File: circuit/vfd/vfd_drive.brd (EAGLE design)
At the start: 92 x 46 mm, 69 parts, among them J1 ZX62R-AB-5P, J2 2DC-0415D200, J3 FSM-21045-10, J5 PSM-210223-10, Q2 MMSS8050-L, Q3 MMSS8050-L, SW1 SKRPACE010, SW2 SKRPACE010, U1 FT231XS, U2 MAX6921AWI+, U3 NJW4131, U4 DS3231M, U5 ADP3338AKCZ-3.3, U6 PSF-A85, U9 BME280

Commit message: [update]update from thinkpad
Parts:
- removed LED3: VBUS, taki-library:CHIPLED_0603
- removed R10: 1k, taki-library:R0603
- moved C12 162.7 mm to (65.5, -17.5)
- moved C16 162.7 mm to (71.5, -17.5)
- moved C17 162.7 mm to (77.0, -17.5)
- moved LED1 162.7 mm to (83.0, 0.00)
- moved LED2 162.7 mm to (66.5, -7.50)
- moved LED4 162.7 mm to (78.0, -0.50)
- moved Q2 162.7 mm to (67.5, -24.0)
- moved Q3 162.7 mm to (67.5, -31.0)
- moved R12 162.7 mm to (75.0, -6.50)
- moved R13 162.7 mm to (79.5, -6.50)
- moved R14 162.7 mm to (84.0, -6.50)
- moved R15 162.7 mm to (70.5, -6.50)
- moved R16 162.7 mm to (65.5, -12.0)
- moved R17 162.7 mm to (70.0, -12.0)
- moved R18 162.7 mm to (74.5, -12.0)
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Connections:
- removed net N$13: LED3.A, R10.1
- removed net N$17: R10.2
- net GND: no longer LED3.C
- net IO0: now also U6.P$10
- net RESET: now also U6.P$24
- net SDA: now also U6.P$5, U6.P$9

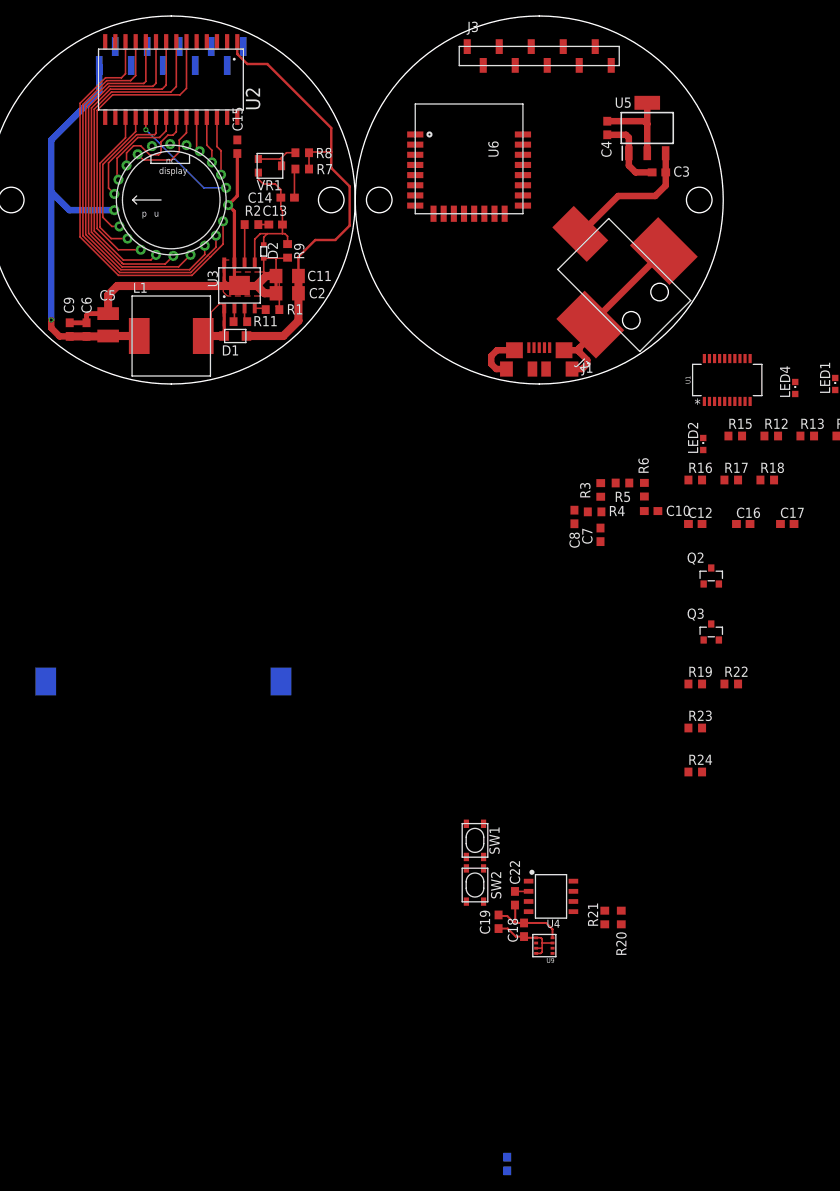
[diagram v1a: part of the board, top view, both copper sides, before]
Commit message: [update]update connector routing
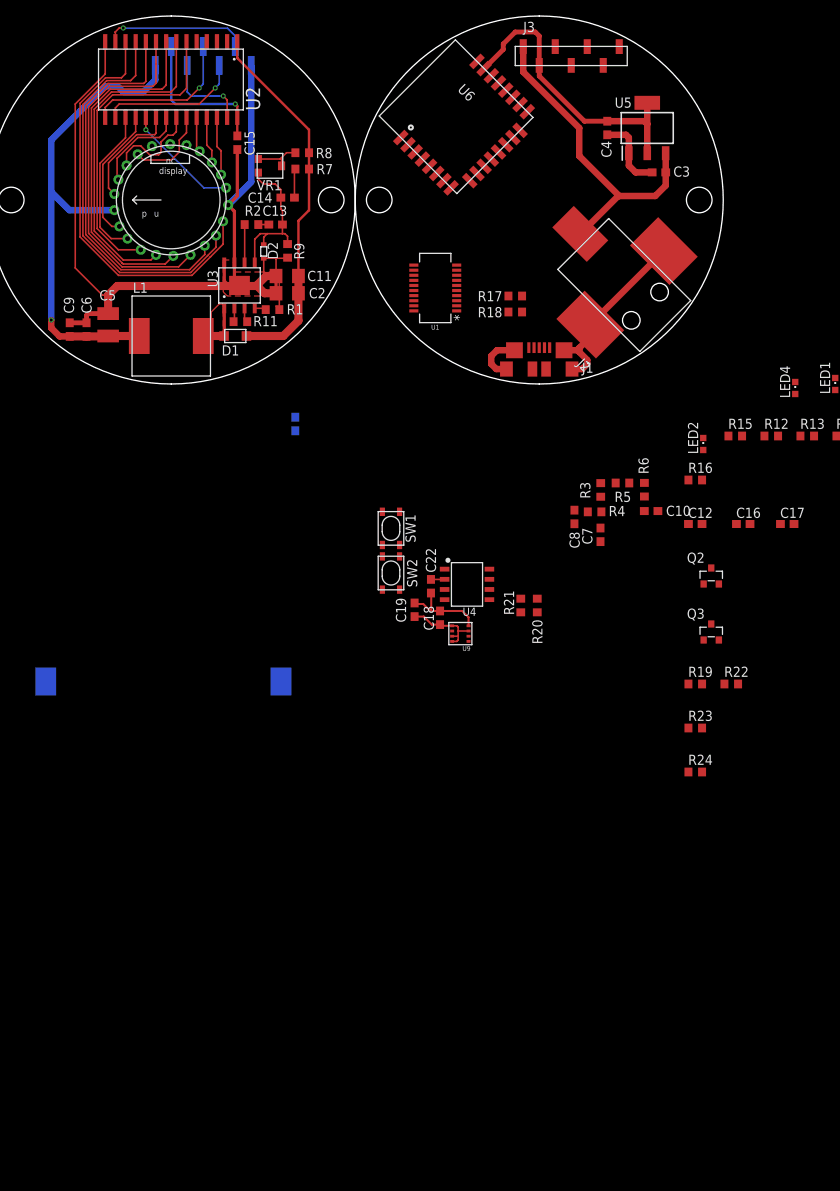
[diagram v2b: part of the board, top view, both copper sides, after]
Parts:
- J3: value FSM-21045-10 -> FSM-21045-7; device taki-library:FSM-21045-10 -> taki-library:FSM-21045-7
- J5: value PSM-210223-10 -> PSM-210223-7; device taki-library:PSM-210223-10 -> taki-library:PSM-210223-7
- moved C1 96.2 mm to (15.5, -5.00), turned to 270 degrees
- moved C22 40.4 mm to (32.5, -25.3)
- moved R20 40.4 mm to (45.8, -27.7)
- moved R21 40.4 mm to (43.7, -27.7)
- moved SW1 40.4 mm to (27.5, -18.0)
- moved SW2 40.4 mm to (27.5, -23.6)
- moved U4 40.4 mm to (37.0, -25.1)
- moved U9 40.4 mm to (36.1, -31.2)
- moved C18 40.4 mm to (33.6, -29.2)
- moved C19 40.4 mm to (30.4, -28.2)
- moved U1 38.3 mm to (33.0, 12.0), turned to 90 degrees
- moved R18 37.9 mm to (43.0, 9.00), turned to 180 degrees
- moved R17 35.5 mm to (43.0, 11.0), turned to 180 degrees
- moved J3 7.00 mm to (44.0, 41.0)
- moved J5 7.00 mm to (-2.00, 41.0)
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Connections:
- net +3V3: now also J3.2
- net +5V: now also J3.1
- net GND: now also J3.7, J5.7
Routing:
- net GND: track 122.3 -> 176.8 mm
- net +5V: track 74.6 -> 105.0 mm
- net +3V3: track 23.9 -> 49.1 mm
- net N$4: track 0.00 -> 19.3 mm, vias 0 -> 1
- net N$2: track 0.00 -> 19.0 mm, vias 0 -> 1
- net N$18: track 0.00 -> 18.2 mm, vias 0 -> 1
- net N$5: track 0.00 -> 17.7 mm, vias 0 -> 1
- net +24V: track 58.4 -> 46.5 mm
- net N$3: track 0.00 -> 10.9 mm, vias 0 -> 1

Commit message: [complete]complete vfd driver board
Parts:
- removed LED4: VBUS, taki-library:CHIPLED_0603
- removed Q3: MMSS8050-L, taki-library:SOT23
- removed R14: 1k, taki-library:R0603
- removed R15: 4.7k, taki-library:R0603
- removed R16, R19, R22: 10k, taki-library:R0603
- removed R4, R6: 470, taki-library:R0603
- added J4: PSM-210223-7, taki-library:PSM-210223-7
- added J6: FSM-21045-7, taki-library:FSM-21045-7
- added Q1: BSS138, taki-library:SOT23-N-MOSFET
- added R10, R25: 4.7k, taki-library:R0603
- C10: value 1000pF -> 0.1uF
- Q2: value MMSS8050-L -> BSS138; device taki-library:SOT23 -> taki-library:SOT23-N-MOSFET
- moved R24 85.9 mm to (25.7, 27.6)
- moved R23 71.1 mm to (35.8, 21.6), turned to 135 degrees
- moved C10 60.9 mm to (40.1, 41.6), turned to 135 degrees
- moved R20 54.7 mm to (31.3, 25.0), turned to 315 degrees
- moved Q2 53.3 mm to (45.5, 24.5)
- moved R21 51.1 mm to (41.3, 23.3), turned to 0 degrees
- moved R13 45.4 mm to (36.7, 8.80), turned to 90 degrees
- moved LED1 44.3 mm to (38.8, 3.49), turned to 180 degrees
- moved R3 44.3 mm to (48.7, 30.8)
- moved R5 44.2 mm to (46.6, 30.7), turned to 90 degrees
- moved U4 42.8 mm to (29.5, 17.1), turned to 90 degrees
- moved C22 42.6 mm to (34.0, 17.3), turned to 90 degrees
- moved C17 42.2 mm to (43.4, 8.02), turned to 180 degrees
- moved C1 41.9 mm to (-13.4, 25.3), flipped to the top
- moved C19 40.0 mm to (30.7, 11.7), turned to 180 degrees
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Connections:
- removed net N$11: LED4.A, R14.1
- removed net N$12: C10.2, R6.1, SW2.S1, SW2.S2
- removed net N$14: R15.1, R16.2, U1.18
- removed net N$15: Q2.B, R19.1
- removed net N$16: Q3.B, R22.1
- removed net N$2: C15.1, J5.2, U2.28
- removed net N$6: C8.2, R4.1, SW1.S1, SW1.S2
- new net 32KHZ: R10.1, U4.1, U6.P$6
- new net SQW: R25.1, U4.3, U6.P$7
- new net SW1: J4.2
- new net SW2: J4.3
- new net SW3: J4.4
- new net SW4: J4.5
- new net VFBLANK: J3.6, U6.P$11
- new net VFCLK: J3.4, U6.P$14
- new net VFDIN: J3.3, U6.P$15
- new net VFLOAD: J3.5, U6.P$13
- net +3V3: now also C10.1, C15.1, J4.1, J5.2, J6.1, R10.2, R25.2, U2.28
- net DTR: now also Q1.G, Q2.S; no longer Q3.E, R19.2
- net GND: now also C10.2, J4.7, J6.7; no longer C10.1, C7.2, C8.1, LED4.C, R16.1, SW1.P1, SW1.P2, SW2.P1, SW2.P2
- net IO0: now also Q2.D; no longer Q3.C, R6.2
- net RESET: now also Q1.D; no longer C7.1, Q2.C, R4.2
- net RTS: now also Q1.S, Q2.G; no longer Q2.E, R22.2
- net SCL: now also U6.P$5
- net SDA: no longer U6.P$5
- net VBATT: now also J4.6
- net VBUS: no longer R14.2, R15.2
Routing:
- net GND: track 176.8 -> 348.4 mm, vias 0 -> 11
- net +3V3: track 49.1 -> 182.4 mm, vias 0 -> 13
- net VBATT: track 0.00 -> 51.5 mm, vias 0 -> 1
- net VFBLANK: track 0.00 -> 36.7 mm, vias 0 -> 2
- net SDA: track 0.00 -> 32.8 mm, vias 0 -> 2
- net SCL: track 0.06 -> 31.2 mm
- net RESET: track 0.00 -> 26.3 mm, vias 0 -> 2
- net TXD: track 0.00 -> 26.0 mm, vias 0 -> 2
- net +5V: track 105.0 -> 129.6 mm
- net 32KHZ: track 0.00 -> 22.5 mm, vias 0 -> 2
- net VFLOAD: track 0.00 -> 22.3 mm, vias 0 -> 2
- net RXD: track 0.00 -> 21.2 mm, vias 0 -> 2
- net N$8: track 0.00 -> 20.4 mm, vias 0 -> 2
- net N$7: track 0.00 -> 20.1 mm, vias 0 -> 2
- net N$2: track 19.0 -> 0.00 mm, vias 1 -> 0
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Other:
- board size 92 x 46 mm -> 92 x 92 mm

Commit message: [update] draw outline
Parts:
- added C20, C21, C23, C24: 1000pF, taki-library:C0603
- added R14, R15, R4, R6: 10k, taki-library:R0603
- added SW3, SW4, SW5, SW6: JTP1230D, taki-library:JTP1230D
- moved SW2 109.9 mm to (85.0, 86.3)
- moved SW1 107.2 mm to (85.0, 79.4)
- moved C7 98.6 mm to (88.2, 82.6), turned to 0 degrees
- moved C8 96.3 mm to (89.1, 77.6), turned to 270 degrees
- moved J6 68.6 mm to (21.5, 40.5)
- moved C4 64.4 mm to (88.0, 87.0)
- moved U5 64.4 mm to (93.0, 87.0)
- moved C3 64.4 mm to (94.5, 81.5)
- moved C22 62.3 mm to (65.0, 71.3)
- moved C18 62.3 mm to (61.7, 62.7)
- moved C10 62.3 mm to (71.1, 95.6)
- moved C12 62.3 mm to (73.1, 68.7)
- moved C16 62.3 mm to (77.4, 62.0)
- moved C17 62.3 mm to (74.4, 62.0)
- moved J1 62.3 mm to (77.0, 55.9)
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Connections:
- new net N$2: BATT1.P, J6.6
- new net SW1-SW: C20.2, J6.2, R4.1, SW3.3, SW3.4
- new net SW2-SW: C21.2, J6.3, R6.1, SW4.3, SW4.4
- new net SW3-SW: C23.2, J6.4, R14.1, SW5.3, SW5.4
- new net SW4-SW: C24.2, J6.5, R15.1, SW6.3, SW6.4
- net +3V3: now also R14.2, R15.2, R4.2, R6.2
- net GND: now also C20.1, C21.1, C23.1, C24.1, C7.2, C8.1, SW1.P1, SW1.P2, SW2.P1, SW2.P2, SW3.1, SW3.2, SW4.1, SW4.2, SW5.1, SW5.2, SW6.1, SW6.2
- net IO0: now also C7.1, SW2.S1, SW2.S2
- net RESET: now also C8.2, SW1.S1, SW1.S2
- net SW1: now also U6.P$19
- net SW2: now also U6.P$18
- net SW3: now also U6.P$17
- net SW4: now also U6.P$16
- net VBATT: no longer BATT1.P
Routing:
- net GND: track 348.4 -> 377.4 mm
- net IO0: track 12.5 -> 30.7 mm, vias 0 -> 4
- net SW4: track 0.00 -> 15.0 mm, vias 0 -> 3
- net RESET: track 26.3 -> 40.9 mm, vias 2 -> 4
- net SW3: track 0.00 -> 11.9 mm, vias 0 -> 1
- net SW1: track 0.00 -> 10.5 mm, vias 0 -> 1
- net SW2: track 0.00 -> 8.37 mm, vias 0 -> 1
- net +3V3: track 182.4 -> 190.2 mm
- net +5V: track 129.6 -> 134.0 mm
- net VFDIN: track 16.5 -> 17.7 mm
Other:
- board size 92 x 92 mm -> 100 x 100 mm
- board text added: "IO0"
- board text added: "RST"

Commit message: [update] update vfd
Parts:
- moved R4 34.5 mm to (30.6, 10.3), turned to 180 degrees
- moved C23 33.2 mm to (41.7, 31.1), turned to 90 degrees
- moved C20 32.6 mm to (41.6, 15.1), turned to 90 degrees
- moved C24 30.3 mm to (4.30, 31.0), turned to 90 degrees
- moved R6 20.7 mm to (16.3, 10.3)
- moved R14 18.4 mm to (32.3, 35.7), turned to 180 degrees
- moved R15 16.1 mm to (13.6, 35.7)
- moved C21 12.7 mm to (4.31, 15.0), turned to 90 degrees
- moved SW5 11.4 mm to (36.5, 31.0), flipped to the bottom
- moved SW3 8.63 mm to (36.5, 15.0), flipped to the bottom
- moved SW4 3.35 mm to (9.50, 15.0), flipped to the bottom
- moved SW6 2.06 mm to (9.50, 31.0), flipped to the bottom
- moved J6 0.71 mm to (21.0, 41.0)
- moved BATT1 0.52 mm to (23.0, 23.0)
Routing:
- net GND: track 377.4 -> 513.0 mm, vias 11 -> 122
- net +3V3: track 190.2 -> 252.8 mm, vias 13 -> 15
- net SW2-SW: track 0.00 -> 54.4 mm, vias 0 -> 3
- net SW1-SW: track 0.00 -> 49.0 mm, vias 0 -> 3
- net SW4-SW: track 0.00 -> 36.5 mm
- net N$2: track 0.00 -> 24.9 mm, vias 0 -> 2
- net SW3-SW: track 0.00 -> 21.6 mm
- added copper zone on layer 16, net GND

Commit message: [add]add silk
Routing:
- net GND: vias 122 -> 131
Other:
- board text added: "Designed by Kinoshita(@_nosita)"
- board text added: "Nostalgy"
- board text added: "nittc meister2018"
- board text added: "vfd tube drive board rev.2"
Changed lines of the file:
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@@
 <dimension x1="23" y1="46" x2="23" y2="54" x3="14" y3="50" textsize="1.778" layer="47"/>
 <dimension x1="23" y1="46" x2="23" y2="0" x3="-8" y3="23" textsize="1.778" layer="47"/>
+<hole x="4" y="85" drill="3.2"/>
+<text x="17.5" y="6.5" size="2.1844" layer="21">Nostalgy</text>
+<text x="13.5" y="4.5" size="1.016" layer="21">Designed by Kinoshita(@_nosita)</text>
+<text x="15.5" y="3" size="1.016" layer="21">vfd tube drive board rev.2</text>
+<text x="18" y="1.5" size="1.016" layer="21">nittc meister2018</text>
 </plain>
 <attributes>
@@
 <via x="4.5" y="73.5" extent="1-16" drill="0.3048"/>
 <via x="4.5" y="81.5" extent="1-16" drill="0.3048"/>
-<via x="4.5" y="85" extent="1-16" drill="0.3048"/>
 <via x="8.5" y="90" extent="1-16" drill="0.3048"/>
 <via x="12" y="93.5" extent="1-16" drill="0.3048"/>
@@
 <vertex x="28.5" y="65.5"/>
 </polygon>
-<wire x1="57.73" y1="72.955" x2="37.54" y2="69.79" width="0" layer="19" extent="1-1"/>
 <via x="13" y="66.5" extent="1-16" drill="0.3048"/>
 <via x="26.5" y="66.5" extent="1-16" drill="0.3048"/>
@@
 <via x="11" y="68" extent="1-16" drill="0.3048"/>
 <via x="4.5" y="71.5" extent="1-16" drill="0.3048"/>
+<via x="69" y="84" extent="1-16" drill="0.3048"/>
+<via x="85.5" y="67.5" extent="1-16" drill="0.3048"/>
+<via x="86.5" y="68" extent="1-16" drill="0.3048"/>
+<via x="87" y="69" extent="1-16" drill="0.3048"/>
+<via x="88" y="68" extent="1-16" drill="0.3048"/>
+<via x="87.5" y="67" extent="1-16" drill="0.3048"/>
+<via x="86.5" y="66.5" extent="1-16" drill="0.3048"/>
+<via x="87.5" y="65.5" extent="1-16" drill="0.3048"/>
+<via x="88.5" y="66" extent="1-16" drill="0.3048"/>
+<via x="89" y="67" extent="1-16" drill="0.3048"/>
+<wire x1="33" y1="42.175" x2="36.5" y2="62" width="0" layer="19" extent="1-1"/>
 </signal>
 <signal name="VBUS">

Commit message: [add]add all
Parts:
- added U$1: (no value), 180118 Library by matsu:HAZAMARU
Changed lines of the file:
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@@
 <dimension x1="23" y1="46" x2="23" y2="54" x3="14" y3="50" textsize="1.778" layer="47"/>
 <dimension x1="23" y1="46" x2="23" y2="0" x3="-8" y3="23" textsize="1.778" layer="47"/>
-<hole x="4" y="85" drill="3.2"/>
+<hole x="5" y="85" drill="3.2"/>
 <text x="17.5" y="6.5" size="2.1844" layer="21">Nostalgy</text>
 <text x="13.5" y="4.5" size="1.016" layer="21">Designed by Kinoshita(@_nosita)</text>
 <text x="15.5" y="3" size="1.016" layer="21">vfd tube drive board rev.2</text>
 <text x="18" y="1.5" size="1.016" layer="21">nittc meister2018</text>
+<hole x="77" y="43" drill="3.2"/>
+<circle x="77" y="43" radius="3" width="0.0762" layer="47"/>
 </plain>
 <attributes>
@@
 <attribute name="NAME" x="3.458" y="29.351" size="1.27" layer="25" rot="R90"/>
 </element>
+<element name="U$1" library="180118 Library by matsu" package="HAZAMARU" value="" x="66.5" y="13" smashed="yes"/>
 </elements>
 <signals>

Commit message: [add]add all
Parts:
- removed BATT1: SMTU2032, taki-library:SMTU2032
- removed C18, C19, C22: 0.1uF, taki-library:C0603
- removed C20, C21, C23, C24: 1000pF, taki-library:C0603
- removed D1: SS2040FL, taki-library:SOD-123FL
- removed D2: BZX584C3V9, taki-library:SOD-523
- removed J2: 2DC-0415D200, taki-library:2DC-0415D200
- removed J4: PSM-210223-7, taki-library:PSM-210223-7
- removed J6: FSM-21045-7, taki-library:FSM-21045-7
- removed LED1: RX, taki-library:CHIPLED_0603
- removed LED2: TX, taki-library:CHIPLED_0603
- removed R12, R13: 1k, taki-library:R0603
- removed R14, R15, R23, R24, R4, R6: 10k, taki-library:R0603
- removed R17, R18: 27, taki-library:R0603
- removed R20, R21, R25: 4.7k, taki-library:R0603
- removed SW1, SW2: SKRPACE010, taki-library:SKRPACE010
- removed SW3, SW4, SW5, SW6: JTP1230D, taki-library:JTP1230D
- removed U$1: (no value), 180118 Library by matsu:HAZAMARU
- removed U4: DS3231M, taki-library:SO08
- removed U9: BME280, taki-library:LGA-8-2.5X2.5
- added J7: DC_JACK_2DC0005D100, taki-library:DC_JACK_2DC0005D100
- added U8: ESP-WROOM-32, taki-library:ESP-WROOM-32
- C10: value 0.1uF -> 5uF
- C12: value 0.1uF -> 1500pF
- C13: value 10uF -> 680pF
- C14: value 270pF -> 100uF; device taki-library:C0603 -> taki-library:C1206
- C16: value 47pF -> 1uF
- C17: value 47pF -> 0.1uF
- C7: value 1000pF -> 1uF
- C8: value 1000pF -> 4.7uF
- L1: value NR10050T470M -> NR10050T221M
- R1: value 27k -> 220
- R10: value 4.7k -> 47k
- R11: value 27k -> 10k
- R2: value 8.2k -> 0.02; device taki-library:R0603 -> taki-library:R1206
- R7: value 27k -> 24k
- U1: value FT231XS -> CP2104; device taki-library:SSOP20_L -> taki-library:QFN24-SILABS
- U3: value NJW4131 -> NJM2360AM; device taki-library:HSOP8 -> taki-library:DMP8
- U6: value PSF-A85 -> RX8035LC; device ITEAD:PSF-A85 -> taki-library:VSOJ12
- moved C17 106.1 mm to (-9.50, -3.00), turned to 0 degrees
- moved C13 64.4 mm to (-25.7, 55.6), turned to 180 degrees
- moved L1 56.1 mm to (-32.5, 68.0)
- moved C2 55.6 mm to (-18.0, 69.3)
- moved C11 55.5 mm to (-18.0, 67.0)
- moved U3 53.7 mm to (-22.0, 62.0)
- moved R1 52.7 mm to (-17.0, 63.3), turned to 270 degrees
- moved R7 49.4 mm to (84.0, 59.7)
- moved R2 45.4 mm to (-7.00, 52.5), turned to 0 degrees
- moved R11 40.2 mm to (71.7, 65.4), turned to 45 degrees
- moved C10 33.0 mm to (73.0, 62.6), turned to 0 degrees
- moved U6 27.5 mm to (84.5, 88.0), turned to 180 degrees
- moved C5 26.8 mm to (-11.6, 59.4), turned to 0 degrees
- moved C7 26.8 mm to (73.0, 60.6)
- moved C8 26.7 mm to (65.8, 64.7), turned to 45 degrees
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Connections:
- removed net 32KHZ: R10.1, U4.1, U6.P$6
- removed net D2_N: R17.2, U1.12
- removed net D2_P: R18.2, U1.11
- removed net D_N1: C16.1, J1.D-, R17.1
- removed net D_P1: C17.1, J1.D+, R18.1
- removed net N$10: LED2.A, R13.1
- removed net N$19: R23.2, U6.P$8
- removed net N$21: R24.1, U6.P$3
- removed net N$40: R1.2, U3.4
- removed net N$41: D1.A, L1.P$2, U3.1
- removed net N$43: R2.2, U3.6
- removed net N$46: C13.1, R2.1
- removed net N$47: C13.2, C14.1, D2.K, R9.2, U3.5, VR1.3
- removed net N$48: C14.2, R7.2
- removed net N$49: R8.2, VR1.1, VR1.2
- removed net RESET: C8.2, Q1.D, R3.1, SW1.S1, SW1.S2, U6.P$24
- removed net RXD: U1.4, U6.P$22
- removed net SQW: R25.1, U4.3, U6.P$7
- removed net SW1: J4.2, U6.P$19
- removed net SW1-SW: C20.2, J6.2, R4.1, SW3.3, SW3.4
- removed net SW2: J4.3, U6.P$18
- removed net SW2-SW: C21.2, J6.3, R6.1, SW4.3, SW4.4
- removed net SW3: J4.4, U6.P$17
- removed net SW3-SW: C23.2, J6.4, R14.1, SW5.3, SW5.4
- removed net SW4: J4.5, U6.P$16
- removed net SW4-SW: C24.2, J6.5, R15.1, SW6.3, SW6.4
- removed net TXD: U1.20, U6.P$21
- removed net VBATT: J4.6, U4.6
- new net D_N: J1.D-, U1.4
- new net D_P: J1.D+, U1.3
- new net EN: C12.1, Q1.D, R3.1, U8.3
- new net ESP32_RX: U1.21, U8.35
- new net ESP32_TX: U1.20, U8.34
- new net N$11: C13.1, U3.3
- new net N$12: R8.2, U3.5, VR1.1, VR1.2
- new net N$13: R1.1, U3.8
- new net N$14: L1.P$1, R1.2, R2.2, U3.7
- new net N$6: L1.P$2, U3.1
- net +24V: no longer D1.K, R7.1
- net +3V3: now also C14.1, C16.1, C7.1, R11.2, U1.5, U1.6, U1.7, U6.2, U8.2; no longer C12.1, C18.1, C19.1, C22.1, J4.1, J6.1, R10.2, R12.2, R13.2, R14.2, R15.2, R20.2, R21.2, R24.2, R25.2, R4.2, R6.2, U1.13, U1.14, U1.15, U1.3, U4.2, U6.P$23, U9.2, U9.5, U9.6, U9.8
- net +5V: now also J7.1, R2.1, U3.6; no longer J2.1, L1.P$1, R11.2, U3.3
- net DTR: now also U1.23; no longer U1.1
- net GND: now also C13.2, C14.2, C8.2, J7.2, J7.3, R10.1, U1.2, U1.25, U3.2, U3.4, U8.1, U8.15, U8.38, U8.GND; no longer BATT1.N, C18.2, C19.2, C20.1, C21.1, C22.2, C23.1, C24.1, C8.1, D2.A, J2.2, J2.3, J4.7, J6.7, R1.1, R23.1, SW1.P1, SW1.P2, SW2.P1, SW2.P2, SW3.1, SW3.2, SW4.1, SW4.2, SW5.1, SW5.2, SW6.1, SW6.2, U1.16, U1.6, U3.7, U3.8, U3.PAD, U4.5, U6.P$12, U6.P$20, U9.1, U9.7
- net IO0: now also U8.25; no longer C7.1, SW2.S1, SW2.S2, U6.P$10
- net N$1: now also R9.2, VR1.3; no longer R11.1, U3.2
- net N$2: now also C17.1, U6.1; no longer BATT1.P, J6.6
- net N$7: now also R11.1, U1.9; no longer LED1.C, U1.17
- net N$8: now also R10.2, R7.1, U1.8; no longer LED2.C, U1.10
- net N$9: now also C8.1, U1.16; no longer LED1.A, R12.1
- net RTS: now also U1.19; no longer U1.2
- net SCL: now also U6.6, U8.36; no longer R20.1, U4.8, U6.P$5, U9.4
- net SDA: now also U6.8, U8.33; no longer R21.1, U4.7, U6.P$9, U9.3
- net VBUS: now also R7.2
- net VFBLANK: no longer U6.P$11
- net VFCLK: no longer U6.P$14
- net VFDIN: no longer U6.P$15
- net VFLOAD: no longer U6.P$13
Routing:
- net GND: track 513.0 -> 208.1 mm, vias 131 -> 30
- net +3V3: track 252.8 -> 103.0 mm, vias 15 -> 4
- net +5V: track 134.0 -> 39.0 mm, vias 2 -> 1
- net SW2-SW: track 54.4 -> 0.00 mm, vias 3 -> 0
- net VBATT: track 51.5 -> 0.00 mm, vias 1 -> 0
- net SW1-SW: track 49.0 -> 0.00 mm, vias 3 -> 0
- net +24V: track 46.4 -> 0.00 mm
- net RESET: track 40.9 -> 0.00 mm, vias 4 -> 0
- net ESP32_RX: track 0.00 -> 39.5 mm, vias 0 -> 2
- net ESP32_TX: track 0.00 -> 39.0 mm, vias 0 -> 2
- net VFBLANK: track 36.7 -> 0.00 mm, vias 2 -> 0
- net SW4-SW: track 36.5 -> 0.00 mm
- net EN: track 0.00 -> 26.8 mm, vias 0 -> 2
- net TXD: track 26.0 -> 0.00 mm, vias 2 -> 0
- net N$2: track 24.9 -> 0.00 mm, vias 2 -> 0
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- removed copper zone on layer 1, net N$41
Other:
- board text removed: "IO0"
- board text removed: "RST"
